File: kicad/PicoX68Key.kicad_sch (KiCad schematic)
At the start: 21 parts, among them J1 LED_BOARD, J2 MINI-DIN-7, Q1 2N7000, Q2 2N7000, Q3 2N7000, U1 Pico

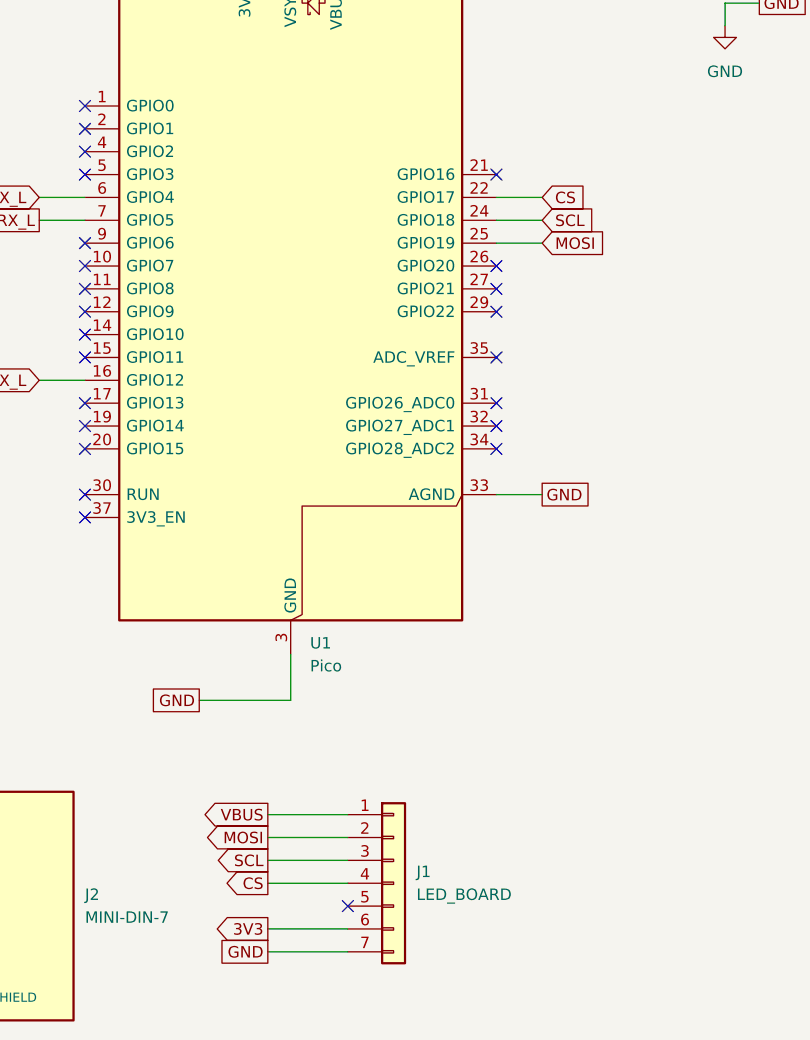
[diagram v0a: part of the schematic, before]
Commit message: Add PWM functionality to set LED brightness
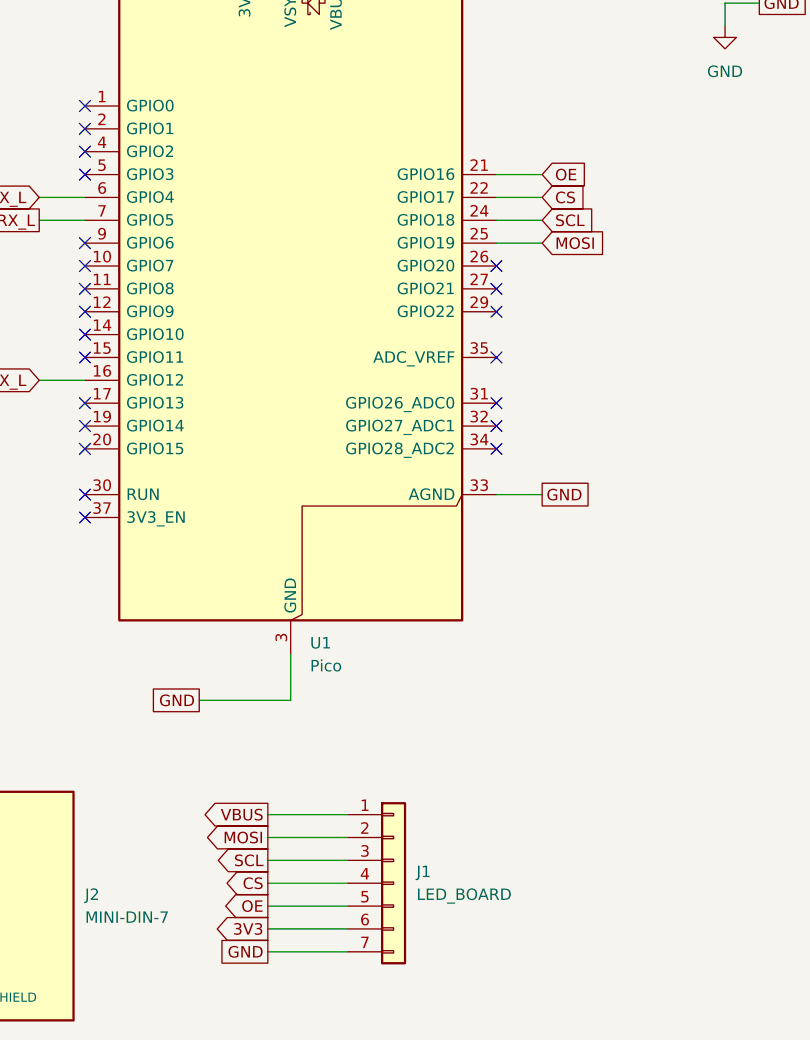
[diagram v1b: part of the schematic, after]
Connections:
- net OE: now reaches J1.5 (Pin_5)
- net OE: now also U1.21 (GPIO16)
- no-connect marks 27 -> 25
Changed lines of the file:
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@@
-	)
-	(no_connect
-		(at 223.52 130.81)
 	)
 	(no_connect
@@
 	)
 	(no_connect
-		(at 240.03 49.53)
-	)
-	(no_connect
 		(at 194.31 57.15)
 	)
@@
 	(wire
 		(pts
+			(xy 214.63 130.81) (xy 223.52 130.81)
+		)
+		(stroke
+			(width 0)
+			(type default)
+		)
+	)
+	(wire
+		(pts
 			(xy 130.81 63.5) (xy 144.78 63.5)
 		)
@@
 		(pts
 			(xy 41.91 111.76) (xy 41.91 102.87)
+		)
+		(stroke
+			(width 0)
+			(type default)
+		)
+	)
+	(wire
+		(pts
+			(xy 240.03 49.53) (xy 245.11 49.53)
 		)
 		(stroke
@@
 		)
 	)
+	(global_label "OE"
+		(shape output)
+		(at 214.63 130.81 180)
+		(fields_autoplaced yes)
+		(effects
+			(font
+				(size 1.27 1.27)
+			)
+			(justify right)
+		)
+		(property "Intersheetrefs" "${INTERSHEET_REFS}"
+			(at 209.1653 130.81 0)
+			(effects
+				(font
+					(size 1.27 1.27)
+				)
+				(justify right)
+				(hide yes)
+			)
+		)
+	)
 	(global_label "KB_RX_H"
 		(shape input)
@@
 			(effects
 				(font
+					(size 1.27 1.27)
+				)
+				(justify left)
+				(hide yes)
+			)
+		)
+	)
+	(global_label "OE"
+		(shape input)
+		(at 245.11 49.53 0)
+		(fields_autoplaced yes)
+		(effects
+			(font
+				(size 1.27 1.27)
+			)
+			(justify left)
+		)
+		(property "Intersheetrefs" "${INTERSHEET_REFS}"
+			(at 250.5747 49.53 0)
+			(effects
+				(font
